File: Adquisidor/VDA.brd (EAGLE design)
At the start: 100 x 90 mm, 135 parts, among them J1 USB-2.0, J2 STEREO-JACK, J3 FTSH-107-01-L-DV-K-A, J4 CONVERT-1X4-2.54MM-MALE_HOLES, J5 F0504-H-05-10G-R, J6 CONVERT-2X7-2.54MM-FEMALE, Q1 BC856, Q2 BC856, SW1 DSHP03TSGER, U1 SN74LVC1G175, U2 CP2102N-28, U3 STM32F373CBT6, U4 LP5907MFX-3.3/NOPB, U5 ISO7721DR, U6 LP5907MFX-3.3/NOPB, U7 TL072, U8 LM13700

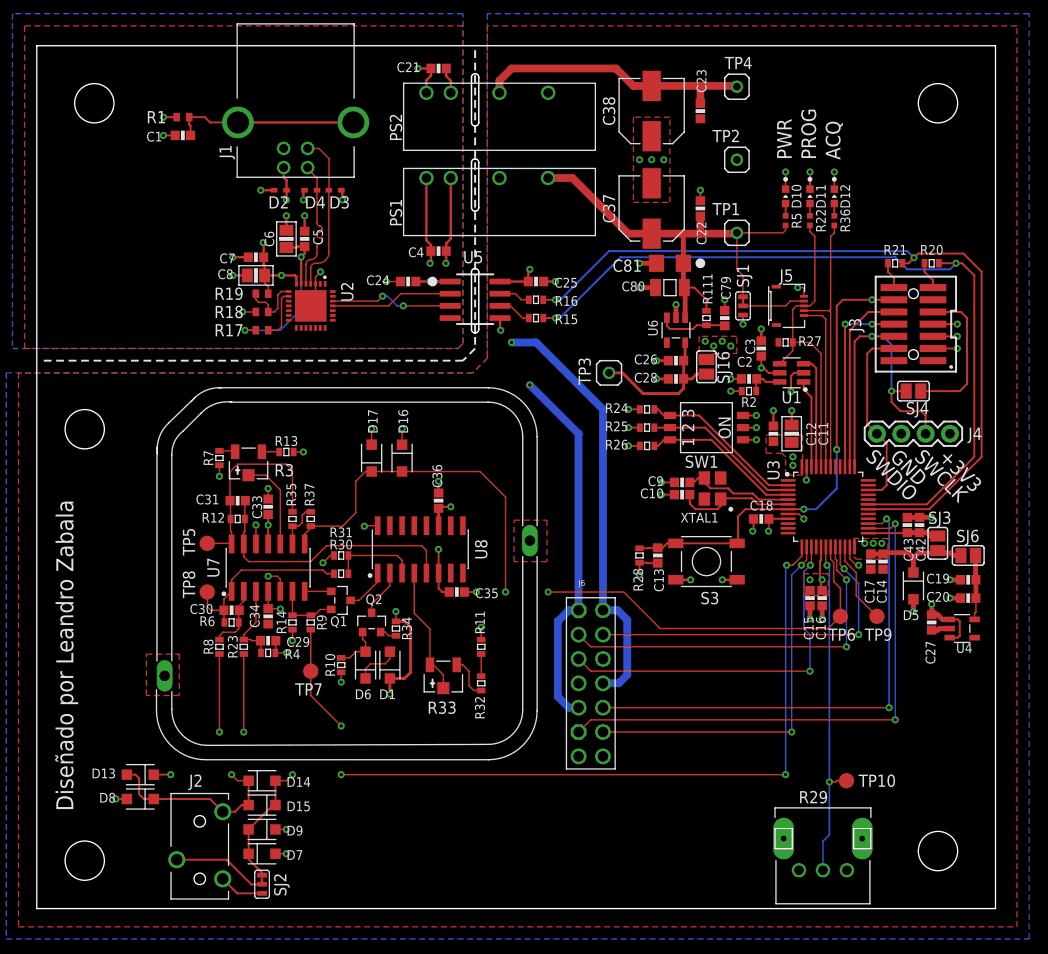
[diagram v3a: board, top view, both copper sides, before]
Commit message: trabajando en los panelizados
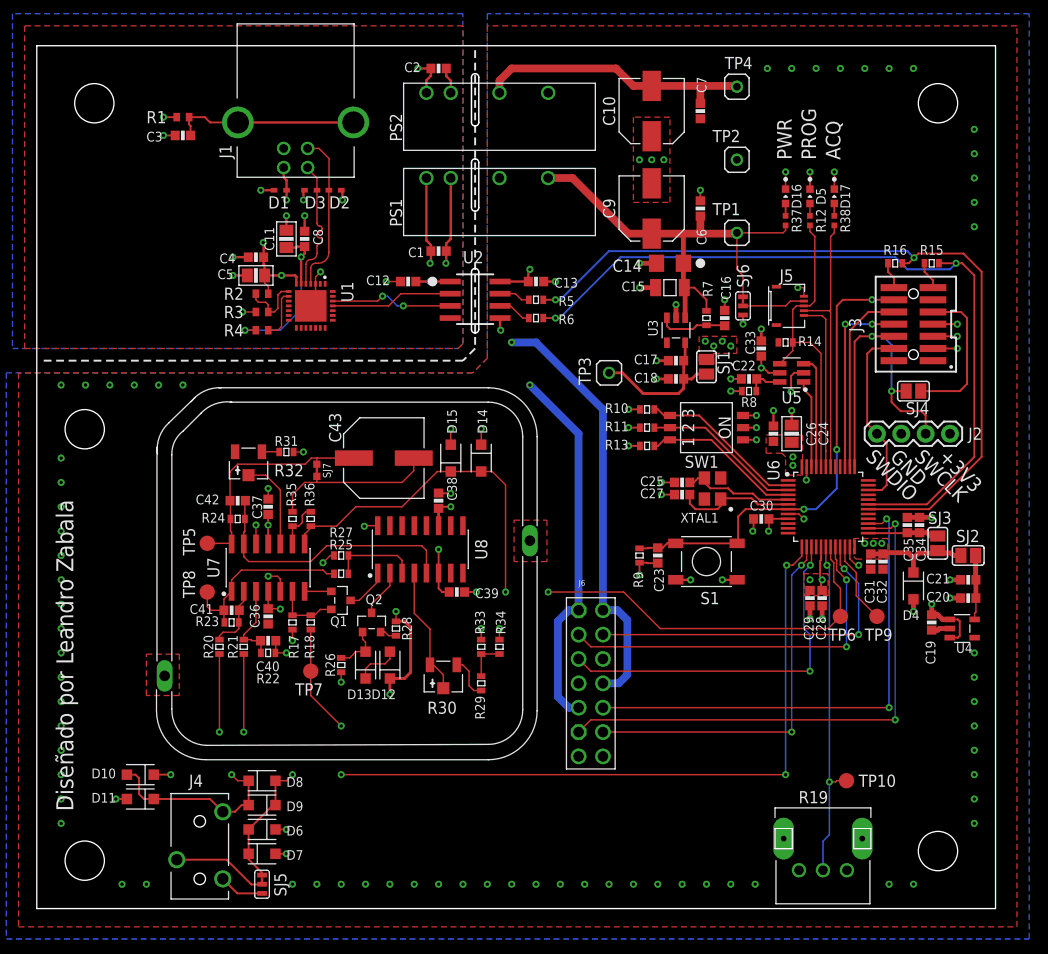
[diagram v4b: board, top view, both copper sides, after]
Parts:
- removed C79: 220n, Property-standar:C_0603
- removed C80: 47u, Property-standar:C_1206
- removed C81: 47u, Property-standar:A_3216
- removed R111: 100k, Property-standar:R_0603
- removed SJ16: (no value), jumper:SJ
- added C32, C39, C40, C41: 100n, Property-standar:C_0603
- added R38: 270, Property-standar:R_0402
- added SJ5: (no value), property-pads:SJ_2S
- added SJ7: SJUMPER-NC, properti-mechanical:SJ1
- C1, C17: value 100n -> 4u7
- C10, C9: value 10p -> 22u; device Property-standar:C_0603 -> Property-standar:CAPAE660X590N
- C11: value 4u7 -> 4.7u
- C14: value 100n -> 47u; device Property-standar:C_0603 -> Property-standar:A_3216
- C15: value 100n -> 47u; device Property-standar:C_0603 -> Property-standar:C_1206
- C16: value 100n -> 220n
- C19: value 100n -> 10u
- C2: value 470n -> 4u7
- C21, C26, C4: value 4u7 -> 100n
- C22: value 100n -> 470n
- C24: value 100n -> 4u7; device Property-standar:C_0603 -> Property-standar:C_0805
- C25: value 100n -> 10p
- C27: value 10u -> 10p
- C31: value 47n -> 100n
- C34: value 100n -> 1u
- C37, C38: value 22u -> 100n; device Property-standar:CAPAE660X590N -> Property-standar:C_0603
- C42: value 1u -> 47n
- C43: value 100n -> DNP; device Property-standar:C_0603 -> Property-standar:CAPAE830X680N
- C5: value 100n -> 4.7u; device Property-standar:C_0603 -> Property-standar:C_0805
- C6, C8: value 4.7u -> 100n; device Property-standar:C_0805 -> Property-standar:C_0603
- D1: value 1N4148 -> LESD5D5.0CT1G; device Property-standar:SOD123W -> property:SOD523
- D10: value GREEN -> 1N4148; device Property-standar:LED_0603_ARROW -> Property-standar:SOD123W
- D11, D12: value ORANGE -> 1N4148; device Property-standar:LED_0603_ARROW -> Property-standar:SOD123W
- D16: value 1N4148 -> GREEN; device Property-standar:SOD123W -> Property-standar:LED_0603_ARROW
- D17: value 1N4148 -> ORANGE; device Property-standar:SOD123W -> Property-standar:LED_0603_ARROW
- D4: value LESD5D5.0CT1G -> D-SOD123W; device property:SOD523 -> Property-standar:SOD123W
- D5: value D-SOD123W -> ORANGE; device Property-standar:SOD123W -> Property-standar:LED_0603_ARROW
- J2: value STEREO-JACK -> CONVERT-1X4-2.54MM-MALE_HOLES; device Connectors:PJ-3200 -> property-connectors:1X04
- J4: value CONVERT-1X4-2.54MM-MALE_HOLES -> STEREO-JACK; device property-connectors:1X04 -> Connectors:PJ-3200
- R10: value 150 -> 10k
- R11, R8: value 100 -> 10k
- R12: value 100k -> 270; device Property-standar:R_0603 -> Property-standar:R_0402
- R13: value TBD -> 10k
- R14: value DNP -> 10k
- R17: value 1k -> DNP; device resistor:R0402 -> Property-standar:R_0603
- R18: value 47.5k -> 33k; device resistor:R0402 -> Property-standar:R_0603
- R19: value 22.1k -> 10k; device resistor:R0402 -> Property-standar:POT-09VR1M
- R2: value 10k -> 22.1k; device Property-standar:R_0603 -> resistor:R0402
- R22: value 270 -> 10M; device Property-standar:R_0402 -> Property-standar:R_0603
- R23: value 100 -> 10M
- R24: value 10k -> 100k
- R25, R28: value 10k -> 1k
- R26: value 10k -> 150
- R27: value 10k -> 2k
- R29: value 10k -> 100; device Property-standar:POT-09VR1M -> Property-standar:R_0603
- R3: value TBD -> 47.5k; device Property-standar:RV3.2X4 -> resistor:R0402
- R30: value 33k -> 500; device Property-standar:R_0603 -> Property-standar:RV3.2X4
- R31: value 3k9 -> 1k
- R32: value 100 -> 500; device Property-standar:R_0603 -> Property-standar:RV3.2X4
- R33: value 500 -> 100; device Property-standar:RV3.2X4 -> Property-standar:R_0603
- R34: value 1k -> DNP
- R36: value 270 -> 2k2; device Property-standar:R_0402 -> Property-standar:R_0603
- R37: value 2k2 -> 270; device Property-standar:R_0603 -> Property-standar:R_0402
- R4: value 10M -> 1k; device Property-standar:R_0603 -> resistor:R0402
- R5: value 270 -> 100; device Property-standar:R_0402 -> Property-standar:R_0603
- R6: value 10M -> 100
- R7: value TBD -> 100k
- R9: value 33k -> 10k
- SJ1, SJ2: device property-pads:SJ_2S -> jumper:SJ
- SJ6: device jumper:SJ -> property-pads:SJ_2S
- U1: value SN74LVC1G175 -> CP2102N-28; device property_digital:SOT-23-6 -> property:MLP28
- U2: value CP2102N-28 -> ISO7721DR; device property:MLP28 -> property_digital:SO8
- U3: value STM32F373CBT6 -> LP5907MFX-3.3/NOPB; device property:QFP50P900X900X160-48N -> property-power:SOT23-5
- U5: value ISO7721DR -> SN74LVC1G175; device property_digital:SO8 -> property_digital:SOT-23-6
- U6: value LP5907MFX-3.3/NOPB -> STM32F373CBT6; device property-power:SOT23-5 -> property:QFP50P900X900X160-48N
- moved D11 94.0 mm to (10.8, 11.4), turned to 180 degrees
- moved D10 90.4 mm to (10.8, 14.0), turned to 180 degrees
- moved J2 85.7 mm to (87.6, 49.5), turned to 0 degrees
- moved J4 85.7 mm to (17.0, 1.00), turned to 90 degrees
- moved R20 84.4 mm to (19.1, 27.3), turned to 270 degrees
- moved R19 83.9 mm to (82.0, 4.00), turned to 270 degrees
- moved SJ2 81.3 mm to (97.2, 36.8), turned to 0 degrees
- moved R21 78.8 mm to (21.6, 27.3), turned to 270 degrees
- moved C21 76.8 mm to (97.2, 34.3), turned to 180 degrees
- moved D4 75.2 mm to (91.4, 33.7), turned to 270 degrees
- moved R22 72.3 mm to (24.1, 26.7), turned to 180 degrees
- moved C42 71.2 mm to (21.0, 42.5), turned to 0 degrees
- moved C34 68.6 mm to (92.1, 40.0), turned to 90 degrees
- moved D12 67.4 mm to (36.8, 25.4), turned to 90 degrees
- moved R12 67.3 mm to (80.6, 71.8), turned to 90 degrees
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- renumbered S3 to S1, SHIELD to SHIELD1
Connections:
- net +3V3: now also C23.P$1, C24.P$1, C26.P$1, C28.P$1, C29.P$1, C33.P$1, D4.A, J2.4, R10.2, R11.2, R13.2, R8.2, R9.2, SJ1.1, SJ6.NO, U5.5, U6.17, U6.48; no longer C11.P$1, C12.P$1, C13.P$1, C15.P$1, C16.P$1, C3.P$1, D5.A, J4.4, R2.2, R24.2, R25.2, R26.2, R28.2, SJ1.NO, SJ16.1, U1.5, U3.17, U3.48
- net +3V3A: now also C30.P$1, C31.P$1, C32.P$1, D14.C, D4.C, R17.2, R19.P$3, R31.2, SJ2.1, U6.24, U6.9; no longer C14.P$1, C17.P$1, C18.P$1, D16.C, D5.C, R13.2, R14.2, R29.P$3, SJ6.1, U3.24, U3.9
- net +5V: now also C13.P$1, C14.A, C15.P$1, C19.P$1, C38.P$1, C6.P$1, C9.+, D10.C, D12.C, D6.C, R28.2, R37.1, R7.2, SJ6.NC, U2.8, U3.1; no longer C22.P$1, C25.P$1, C27.P$1, C34.P$1, C37.+, C80.P$1, C81.A, D1.C, D13.C, D9.C, R111.2, R34.2, R5.1, SJ1.NC, U5.8, U6.1
- net -5V: now also C10.-, C37.P$2, C39.P$2, C7.P$2, D11.A; no longer C23.P$2, C33.P$2, C35.P$2, C38.-, D8.A
- net ACQ_LED: now also R38.1, U6.42; no longer R36.1, U3.42
- net BOOT0: now also R12.1, R14.1, U5.4, U6.44; no longer R22.1, R27.1, U1.4, U3.44
- net DAC1_CH1: now also R18.2, U6.13; no longer R9.2, U3.13
- net DAC1_CH2: now also U6.14; no longer U3.14
- net DAC2_CH1: now also U6.15; no longer U3.15
- net FF_CLK: now also U5.1, U6.46; no longer U1.1, U3.46
- net FF_CLR: now also C22.P$1, R8.1, U5.6; no longer C2.P$1, R2.1, U1.6
- net FF_D: now also U5.3, U6.45; no longer U1.3, U3.45
- net GND: now also C10.+, C13.P$2, C14.K, C21.P$2, C24.P$2, C30.P$2, C31.P$2, C32.P$2, C33.P$2, C35.P$2, C37.P$1, C38.P$2, C39.P$1, C40.P$2, C6.P$2, C7.P$1, C9.-, D15.A, D16.K, D17.K, D5.K, J2.2, J4.1, R14.2, R19.P$1, R22.1, R26.1, R32.3, R33.2, R34.2, SJ5.NO, U2.5, U3.2, U5.2, U6.23, U6.47, U6.8; no longer C10.P$2, C11.P$2, C12.P$2, C14.P$2, C2.P$2, C23.P$1, C3.P$2, C33.P$1, C35.P$1, C37.-, C38.+, C42.P$2, C43.P$2, C79.P$2, C80.P$2, C81.K, C9.P$2, D10.K, D11.K, D12.K, D17.A, J2.1, J4.2, R10.1, R11.2, R29.P$1, R31.2, R4.1, R7.1, SJ2.NO, U1.2, U3.23, U3.47, U3.8, U5.5, U6.2
- net GND-1: now also C11.P$2, C12.P$2, C2.P$2, C3.P$2, D1.C, R3.2, U1.3, U1.EXP, U2.4; no longer C21.P$2, C24.P$2, C6.P$2, C7.P$2, D4.C, R18.2, U2.3, U2.EXP, U5.4
- net JCLK: now also J2.3, U6.37; no longer J4.3, U3.37
- net JTDI: now also U6.38; no longer U3.38
- net JTDO: now also U6.39; no longer U3.39
- net JTMS: now also J2.1, U6.34; no longer J4.1, U3.34
- net MCU_RX: now also R15.2; no longer R20.2
- net MCU_TX: now also R16.2; no longer R21.2
- net N$1: now also C17.P$1, C18.P$1, SJ1.2, U3.5; no longer C26.P$1, C28.P$1, SJ16.2, U6.5
- net N$11: now also R28.1; no longer R34.1
- net N$12: now also D12.A, D13.C; no longer D1.A, D6.C
- net N$13: now also R31.1, R32.1; no longer R13.1, R3.1
- net N$14: now also D16.A, R37.2; no longer D10.A, R5.2
- net N$15: now also D5.A, R12.2; no longer D11.A, R22.2
- net N$16: now also D10.A, D11.C, D9.A, J4.2, R20.2; no longer D13.A, D14.C, D15.A, J2.2, R8.2
- net N$17: now also D6.A, D8.A, D9.C, R21.2, SJ5.NC; no longer D14.A, D15.C, D9.A, R23.2, SJ2.NC
- net N$18: now also R32.2; no longer R3.2
- net N$19: now also R25.2, R27.1; no longer R30.2, R31.1
- net N$2: now also C42.P$1, C43.1, R24.2, SJ7.P$1; no longer C31.P$1, R12.2, R35.1
- net N$20: now also R30.2, R30.3; no longer R33.2, R33.3
- net N$22: now also R29.1, R30.1; no longer R32.1, R33.1
- net N$23: now also SJ6.COM; no longer SJ1.COM
- net N$24: now also D13.A, R26.2; no longer D6.A, R10.2
- net N$27: now also R36.1; no longer R37.1
- net N$3: now also C40.P$1, R21.1, R22.2; no longer C29.P$1, R23.1, R4.2
- net N$4: now also C41.P$1, R20.1, R23.2; no longer C30.P$1, R6.2, R8.1
- net N$46: now also C16.P$1, R7.1, U3.3; no longer C79.P$1, R111.1, U6.3
- net N$5: now also C43.2, R35.1, SJ7.P$2; no longer R3.3, R7.2
- net N$50: now also C21.P$1, SJ2.2; no longer C19.P$1, SJ6.2
- net N$54: now also R4.2, U1.9; no longer R17.2, U2.9
- net N$6: now also J4.3, SJ5.COM; no longer J2.3, SJ2.COM
- net N$7: now also R17.1, R18.1; no longer R14.1, R9.1
- net N$8: now also D17.A, R38.2; no longer D12.A, R36.2
- net N$9: now also R29.2, R33.1, R34.1; no longer R11.1, R32.2
- net NRST: now also C23.P$2, R9.1, U6.7; no longer C13.P$2, R28.1, U3.7
- net OSC2_IN: now also C25.P$1, U6.5; no longer C9.P$1, U3.5
- net OSC2_OUT: now also C27.P$1, U6.6; no longer C10.P$1, U3.6
- net OUT_CHARGE_AMP: now also C41.P$2, R23.1, R25.1; no longer C30.P$2, R30.1, R6.1
- net OUT_OTA: now also C42.P$2, R24.1; no longer C31.P$2, R12.1
- net POWER_LED: now also U6.43; no longer U3.43
- net RXD: now also U1.25, U2.2; no longer U2.25, U5.2
- net SDADC1_CH4: now also U6.20; no longer U3.20
- net SDADC1_CH5: now also D14.A, D15.C, R36.2, U6.19; no longer D16.A, D17.C, R37.2, U3.19
- net SDADC1_CH6: now also R19.P$2, U6.18; no longer R29.P$2, U3.18
- net SDADC1_CH7: now also U6.22; no longer U3.22
- net SDADC1_CH8: now also U6.21; no longer U3.21
- net SDADC3_CH7: now also U6.27; no longer U3.27
- net SDADC3_CH8: now also U6.26; no longer U3.26
- net SHIELD: now also C3.P$1; no longer C1.P$1
- net SW_1: now also R10.1, U6.2; no longer R24.1, U3.2
- net SW_2: now also R11.1, U6.3; no longer R25.1, U3.3
- net SW_3: now also R13.1, U6.4; no longer R26.1, U3.4
- net TXD: now also U1.26, U2.3; no longer U2.26, U5.3
- net USART_RX: now also R15.1, R6.2, U6.31; no longer R15.2, R20.1, U3.31
- net USART_TX: now also R16.1, R5.2, U6.30; no longer R16.2, R21.1, U3.30
- net USB_DET: now also R2.1, R3.1, U1.8; no longer R18.1, R19.1, U2.8
- net USB_DN: now also D3.A, U1.5; no longer D4.A, U2.5
- net USB_DP: now also D2.A, U1.4; no longer D3.A, U2.4
- net USB_RXD: now also R5.1, U2.7; no longer R16.1, U5.7
- net USB_TXD: now also R6.1, U2.6; no longer R15.1, U5.6
- net VBAT: now also U6.1; no longer U3.1
- net VDD_BRIDGE: now also C11.P$1, C8.P$1, R4.1, U1.6; no longer C5.P$1, C6.P$1, R17.1, U2.6
- net VREF_SDADC: now also C34.P$1, C35.P$1, U6.25; no longer C42.P$1, C43.P$1, U3.25
- net VUSB: now also C1.P$1, C12.P$1, C2.P$1, C5.P$1, D1.A, R2.2, U1.7, U2.1; no longer C21.P$1, C24.P$1, C7.P$1, C8.P$1, D2.A, R19.2, U2.7, U5.1
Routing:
- net N$5: track 1.68 -> 17.4 mm
- net N$2: track 21.6 -> 24.3 mm
- net N$9: track 2.31 -> 4.22 mm
- net SDADC1_CH5: track 82.4 -> 81.3 mm
- net GND: track 81.0 -> 80.9 mm, vias 50 -> 116

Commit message: BOM del adquisidor listo
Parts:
- C1, C17, C2, C20: value 4u7 -> 4.7u; device Property-standar:C_0603 -> Property-standar:C_0805
- C19: value 10u -> 4.7u; device Property-standar:C_0603 -> Property-standar:C_0805
- C22: value 470n -> 220n
- C40, C41: device Property-standar:C_0603 -> Property-standar:C_1206
- R12, R37, R38: device Property-standar:R_0402 -> Property-standar:R_0603
- U7: value TL072 -> TL074
- moved C1 19.0 mm to (41.9, 87.6)
- moved C2 19.0 mm to (41.9, 68.6)
- moved C40 2.62 mm to (24.8, 25.4)
- moved R21 2.54 mm to (21.6, 24.8)
- moved R20 1.91 mm to (19.1, 25.4)
- moved R23 1.90 mm to (20.3, 27.9)
- moved C41 1.42 mm to (19.7, 29.8)
- moved C19 0.90 mm to (92.7, 29.2)
- moved C20 0.64 mm to (96.5, 32.4)
- moved C21 0.64 mm to (96.5, 34.3)
- moved R22 0.63 mm to (24.1, 27.3)
- moved D4 0.63 mm to (90.8, 33.7)
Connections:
- net +5V: now also D12.A; no longer D12.C
- net N$12: now also D12.C, D13.A; no longer D12.A, D13.C
- net N$24: now also D13.C; no longer D13.A
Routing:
- net N$12: track 4.74 -> 0.00 mm
- net VUSB: track 31.4 -> 27.2 mm, vias 6 -> 4
- net OUT_CHARGE_AMP: track 19.5 -> 23.0 mm
- net GND: track 80.9 -> 83.9 mm, vias 116 -> 118
- net +5V: track 388.5 -> 385.6 mm, vias 9 -> 8
- net N$17: track 30.3 -> 27.8 mm
- net N$4: track 6.83 -> 8.86 mm
- net N$24: track 4.98 -> 3.00 mm
- net N$16: track 33.2 -> 31.3 mm
- net N$1: track 16.3 -> 14.4 mm
- net GND-1: track 31.0 -> 29.8 mm, vias 13 -> 12
- net N$3: track 8.64 -> 9.67 mm

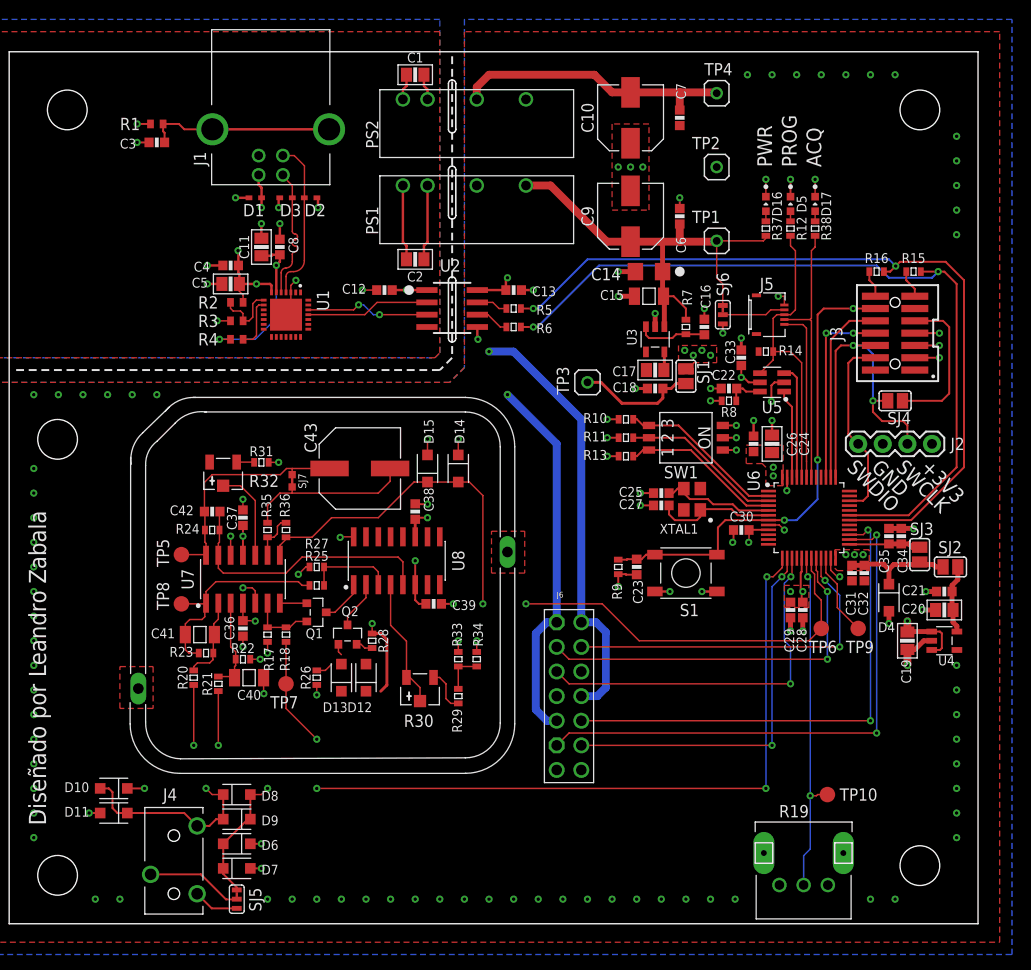
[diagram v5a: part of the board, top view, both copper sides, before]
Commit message: retoques en capa tnames del adquisidor
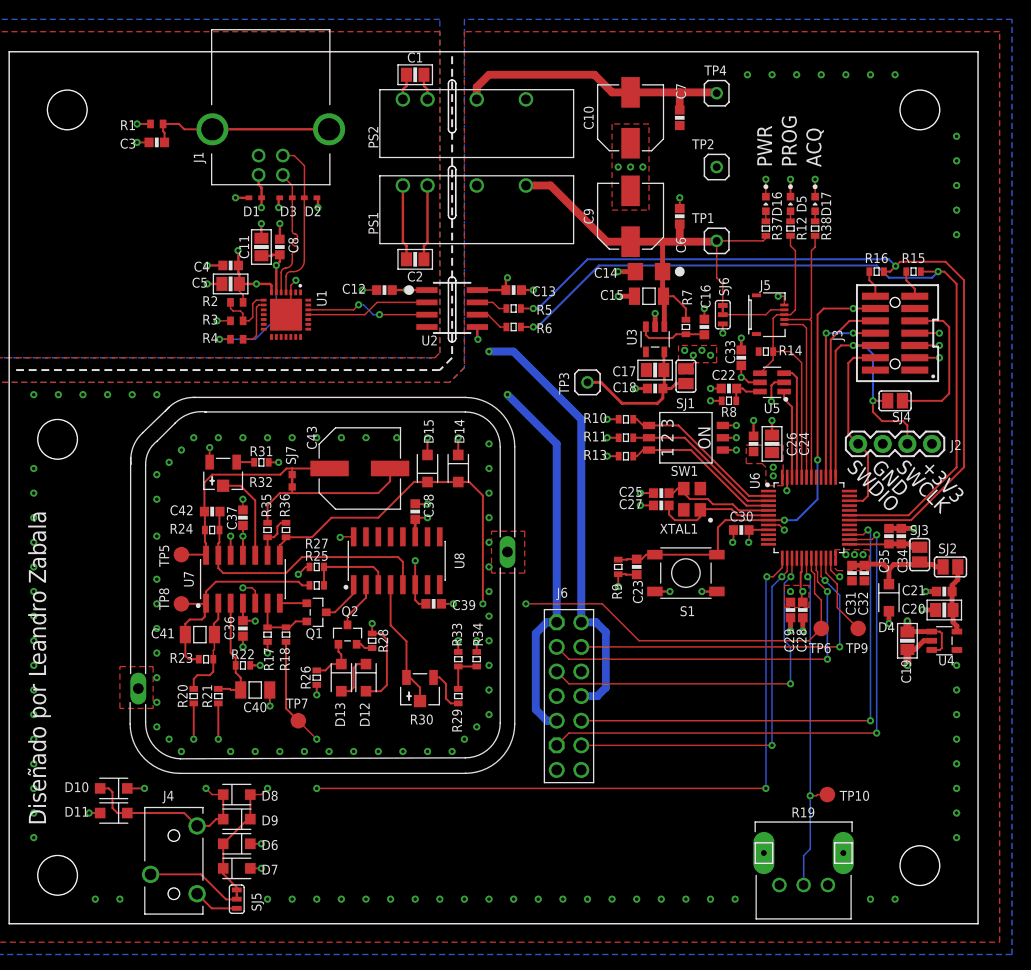
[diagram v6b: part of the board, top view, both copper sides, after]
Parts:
- moved TP7 4.02 mm to (29.8, 21.0)
- moved R20 1.90 mm to (19.1, 23.5)
- moved C40 1.42 mm to (25.4, 24.1)
- moved R21 1.27 mm to (21.6, 23.5)
- moved R23 0.64 mm to (20.3, 27.3)
- moved R22 0.63 mm to (24.1, 26.7)
- turned D12 to 270 degrees
- turned D13 to 270 degrees
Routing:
- net N$12: track 0.00 -> 4.89 mm
- net N$3: track 9.67 -> 11.7 mm
- net N$1: track 14.4 -> 16.5 mm
- net N$24: track 3.00 -> 4.98 mm
- net N$16: track 31.3 -> 29.4 mm
- net N$4: track 8.86 -> 10.7 mm
- net +5V: track 385.6 -> 387.4 mm
- net GND: track 83.9 -> 85.5 mm, vias 118 -> 166
- net N$17: track 27.8 -> 26.5 mm
- net OUT_CHARGE_AMP: track 23.0 -> 23.5 mm
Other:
- board text added: "V: 1.1.__"
